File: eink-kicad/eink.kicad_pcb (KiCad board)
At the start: 2 copper layers, 34.3 x 68.6 mm, 71 parts, among them P1 CONN_1, P13 CONN_1, P14 CONN_1, P15 CONN_1, P16 CONN_1, P17 CONN_1, P18 CONN_1, P19 CONN_1, P2 CONN_1, P20 CONN_1, P21 CONN_1, P22 CONN_1, P23 CONN_1, P24 CONN_1, P25 CONN_1, P26 CONN_1, P27 CONN_1, P28 CONN_1, P3 CONN_1, P30 CONN_1, P31 CONN_1, P32 CONN_1, P33 CONN_1, P35 CONN_1, P36 CONN_1, P37 CONN_1, P38 CONN_1, P39 CONN_1, P4 CONN_1, P40 CONN_1, P5 CONN_1, Q1 MOS_P, U1 LT1945, U2 LM358, U3 78L15, U4 79L15, U5 ED060SC4V2-FPC

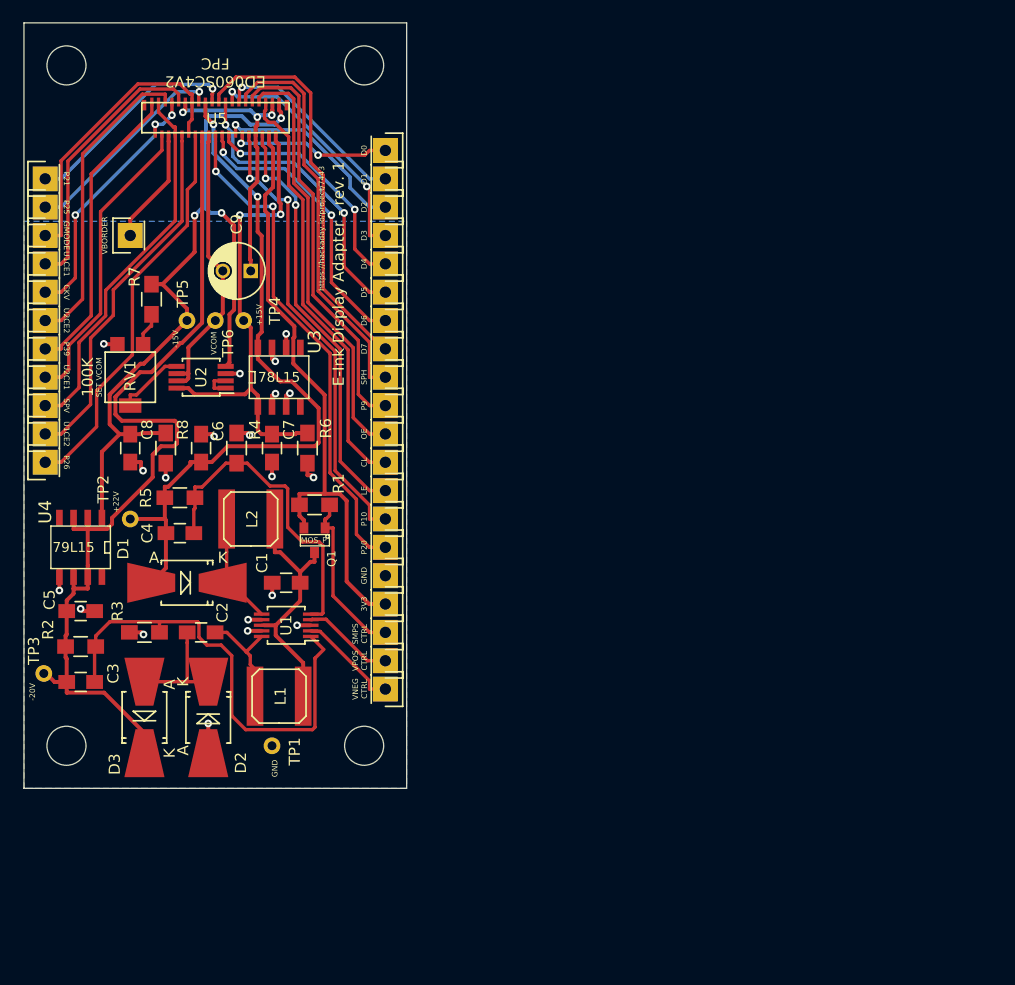
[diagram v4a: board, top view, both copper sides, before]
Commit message: Revision 2 of board with shift registers.
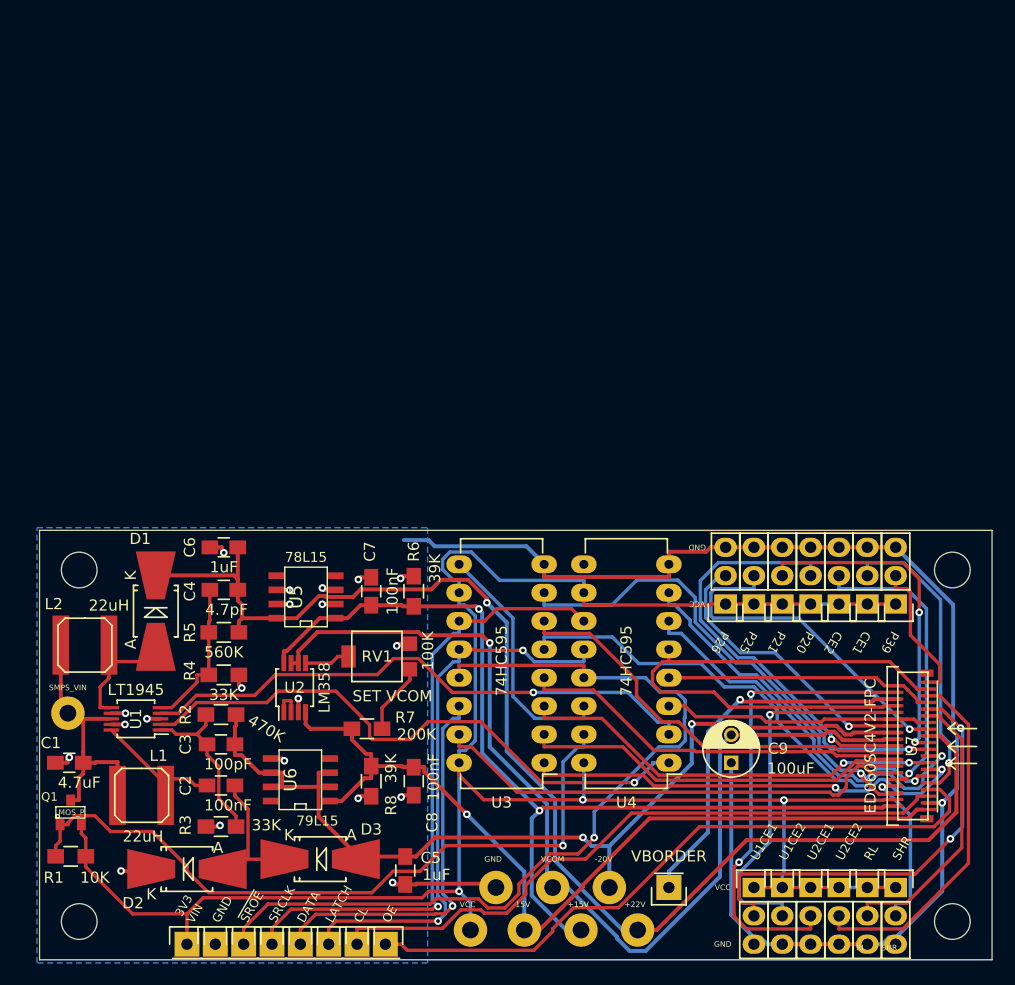
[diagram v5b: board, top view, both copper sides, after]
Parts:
- removed P13, P14, P15, P16, P17, P18, P19, P20, P21, P22, P23, P24, P25, P26, P27, P28, P30, P31, P32, P33, P35, P36, P37, P38, P39, P4, P40, eP34: CONN_1, Pin_Headers:Pin_Header_Straight_1x01
- removed REF** (x4): MountingHole_3-5mm, Mounting_Holes:MountingHole_3-5mm
- removed TP1, TP2, TP3, TP4, TP5, TP6: CONN_1, Measurement_Points:Measurement_Point_Round-TH_Small
- added MNT1: MountingHole_3.2mm_M3, Mounting_Holes:MountingHole_3.2mm_M3, F.Cu at (81.8, 113.8)
- added MNT2: MountingHole_3.2mm_M3, Mounting_Holes:MountingHole_3.2mm_M3, F.Cu at (160.0, 113.8)
- added MNT3: MountingHole_3.2mm_M3, Mounting_Holes:MountingHole_3.2mm_M3, F.Cu at (160.0, 145.3)
- added MNT4: MountingHole_3.2mm_M3, Mounting_Holes:MountingHole_3.2mm_M3, F.Cu at (81.8, 145.3)
- added P10: CONN_01X01, Pin_Headers:Pin_Header_Straight_1x01, F.Cu at (91.4, 147.3)
- added P6: CONN_01X01, Pin_Headers:Pin_Header_Straight_1x01, F.Cu at (96.5, 147.3)
- added P7: CONN_1, Pin_Headers:Pin_Header_Straight_1x01, F.Cu at (106.7, 147.3)
- added P8: CONN_1, Pin_Headers:Pin_Header_Straight_1x01, F.Cu at (109.2, 147.3)
- added P9: CONN_1, Pin_Headers:Pin_Header_Straight_1x01, F.Cu at (134.6, 142.2)
- added SW1: SW_SPDT_Small, Pin_Headers:Pin_Header_Straight_1x03, F.Cu at (154.9, 142.2)
- added SW10: SW_SPDT_Small, Pin_Headers:Pin_Header_Straight_1x03, F.Cu at (142.2, 142.2)
- added SW11: SW_SPDT_Small, Pin_Headers:Pin_Header_Straight_1x03, F.Cu at (149.9, 142.2)
- added SW12: SW_SPDT_Small, Pin_Headers:Pin_Header_Straight_1x03, F.Cu at (147.3, 142.2)
- added SW13: SW_SPDT_Small, Pin_Headers:Pin_Header_Straight_1x03, F.Cu at (154.9, 116.8)
- added SW2: SW_SPDT_Small, Pin_Headers:Pin_Header_Straight_1x03, F.Cu at (152.4, 116.8)
- added SW3: SW_SPDT_Small, Pin_Headers:Pin_Header_Straight_1x03, F.Cu at (149.9, 116.8)
- added SW4: SW_SPDT_Small, Pin_Headers:Pin_Header_Straight_1x03, F.Cu at (147.3, 116.8)
- added SW5: SW_SPDT_Small, Pin_Headers:Pin_Header_Straight_1x03, F.Cu at (144.8, 116.8)
- added SW6: SW_SPDT_Small, Pin_Headers:Pin_Header_Straight_1x03, F.Cu at (142.2, 116.8)
- added SW7: SW_SPDT_Small, Pin_Headers:Pin_Header_Straight_1x03, F.Cu at (139.7, 116.8)
- added SW8: SW_SPDT_Small, Pin_Headers:Pin_Header_Straight_1x03, F.Cu at (152.4, 142.2)
- added SW9: SW_SPDT_Small, Pin_Headers:Pin_Header_Straight_1x03, F.Cu at (144.8, 142.2)
- added U6: 79L15, eink-footprints:79LxxA, F.Cu at (101.6, 132.6)
- added U7: ED060SC4V2-FPC, eink-footprints:FH26-39S-0.3SHW-biggerpads, F.Cu at (157.5, 135.3)
- added W1: TEST_1P, Measurement_Points:Measurement_Point_Round-TH_Big, F.Cu at (80.8, 126.6)
- added W2: TEST_1P, Measurement_Points:Measurement_Point_Round-TH_Big, F.Cu at (119.1, 142.2)
- added W3: TEST_1P, Measurement_Points:Measurement_Point_Round-TH_Big, F.Cu at (116.8, 146.1)
- added W4: TEST_1P, Measurement_Points:Measurement_Point_Round-TH_Big, F.Cu at (121.7, 146.1)
- added W5: TEST_1P, Measurement_Points:Measurement_Point_Round-TH_Big, F.Cu at (126.7, 146.1)
- added W6: TEST_1P, Measurement_Points:Measurement_Point_Round-TH_Big, F.Cu at (124.2, 142.2)
- added W7: TEST_1P, Measurement_Points:Measurement_Point_Round-TH_Big, F.Cu at (131.8, 146.1)
- added W8: TEST_1P, Measurement_Points:Measurement_Point_Round-TH_Big, F.Cu at (129.3, 142.2)
- D1, D2, D3: value DIODESCH -> D_Schottky
- P2, P3, P5: value CONN_1 -> CONN_01X01
- U3: value 78L15 -> 74HC595; footprint eink-footprints:78LxxA -> Housings_DIP:DIP-16_W7.62mm_LongPads
- U4: value 79L15 -> 74HC595; footprint eink-footprints:79LxxA -> Housings_DIP:DIP-16_W7.62mm_LongPads
- U5: value ED060SC4V2-FPC -> 78L15; footprint eink-footprints:FH26-39S-0.3SHW -> eink-footprints:78LxxA
- moved C9 61.6 mm to (140.2, 131.1), turned to 90 degrees
- moved U4 56.1 mm to (134.6, 131.1)
- moved U5 44.0 mm to (102.1, 116.2), turned to 90 degrees
- moved R7 43.1 mm to (107.6, 128.0), turned to 180 degrees
- moved U3 41.9 mm to (123.4, 131.1), turned to 180 degrees
- moved C8 39.2 mm to (111.8, 132.7)
- moved R1 38.3 mm to (81.0, 139.4), turned to 180 degrees
- moved C5 37.2 mm to (111.0, 140.7), turned to 270 degrees
- moved R8 35.1 mm to (108.0, 132.7)
- moved P1 34.1 mm to (94.0, 147.3), turned to 0 degrees
- moved P2 33.9 mm to (101.6, 147.3), turned to 0 degrees
- moved RV1 33.4 mm to (108.5, 121.5), turned to 90 degrees
- moved Q1 32.7 mm to (81.0, 135.5), turned to 0 degrees
- moved U2 29.0 mm to (101.1, 124.3), turned to 90 degrees
- moved P5 28.4 mm to (104.1, 147.3), turned to 0 degrees
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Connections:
- D1 pad 1: /SW2 -> /+22V
- D1 pad 2: /+22V -> /SW2
- D2 pad 1: Net-(C2-Pad2) -> GND
- D2 pad 2: GND -> Net-(C2-Pad2)
- D3 pad 1: /-20V -> Net-(C2-Pad2)
- D3 pad 2: Net-(C2-Pad2) -> /-20V
- P1 pad 1: /+3.3V -> GND
- P2 pad 1: GND -> /SRDATA
- P3 pad 1: /VNEG_CTRL -> /SRCLK
- P5 pad 1: /SMPS_CTRL -> /LATCH
- Q1 pad S: /+3.3V -> VCC
- R1 pad 1: /+3.3V -> VCC
- U3 pad 4: (no net) -> /D4
- U3 pad 5: (no net) -> /D5
- U4 pad 4: (no net) -> /CKV
- U4 pad 8: (no net) -> GND
- U5 pad 4: /+3.3V -> (no net)
- U5 pad 5: /CL -> (no net)
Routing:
- net VCC: track 0.00 -> 188.7 mm, vias 0 -> 3
- net GND: track 52.8 -> 156.1 mm, vias 23 -> 21
- net /~SROE~: track 0.00 -> 77.5 mm, vias 0 -> 1
- net /VCOM: track 25.9 -> 93.1 mm, vias 0 -> 1
- net /SRCLK: track 0.00 -> 56.3 mm, vias 0 -> 1
- net /+3.3V: track 54.2 -> 0.00 mm
- net /+22V: track 63.5 -> 117.4 mm, vias 2 -> 1
- net /LATCH: track 0.00 -> 50.2 mm, vias 0 -> 2
- net /SMPS_CTRL: track 15.1 -> 64.4 mm, vias 0 -> 1
- net /+15V: track 42.8 -> 86.8 mm
- net /VNEG_CTRL: track 9.28 -> 52.9 mm, vias 0 -> 1
- net /VPOS_CTRL: track 8.25 -> 51.0 mm, vias 0 -> 1
- net /P10: track 41.3 -> 0.00 mm, vias 2 -> 0
- net /P9: track 37.1 -> 0.00 mm
- net /SRDATA: track 0.00 -> 35.0 mm, vias 0 -> 1
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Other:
- board size 34.3 x 68.6 mm -> 85.3 x 38.5 mm
- board text added: "3V3 VIN"
- board text added: "470K"
- board text added: "CE1"
- board text added: "CE2"
- board text added: "DATA"
- board text added: "E-Ink Display Adapter - rev. 2"
- board text added: "LATCH"
- board text added: "RL"
- board text added: "SHR"
- board text added: "SMPS_VIN"
- board text added: "SRCLK"
- board text added: "VCC"
- board text added: "~SROE~"
- board text removed: "3V3"
- board text removed: "CKV"
- board text removed: "D0"
- board text removed: "D1"
- board text removed: "D2"
- board text removed: "D3"
- board text removed: "D4"
- board text removed: "D5"
- board text removed: "D6"
- board text removed: "D7"
- board text removed: "E-Ink Display Adapter - rev. 1"
- board text removed: "ED060SC4V2 FPC"
- board text removed: "GMODE"
- board text removed: "LE"
- board text removed: "P10"
- board text removed: "P9"
- board text removed: "SMPS CTRL"
- board text removed: "SPH"
- board text removed: "SPV"
- board text removed: "VNEG CTRL"
- board text removed: "VPOS CTRL"
